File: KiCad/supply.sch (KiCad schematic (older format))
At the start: 61 parts, among them IC12 74HC00PW, IC13 SN74LVC1G126DCKR, IC4 TPS7A0518PDBVT, T3 BSS138APW, U1 LM60440AQRPKRQ1, U2 LM60440AQRPKRQ1

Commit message: Move ethernet connector closet to the edge. Loclib
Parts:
- C16, C17, C18, C19, C20, C21: footprint antmicro-footprints:0805-cap -> jetson-nano-baseboard-footprints:0805-cap; symbol antmicroCapacitorsmisc:C_47u_0805 -> jetson-nano-baseboard:C_47u_0805
- C60: footprint antmicro-footprints:0402-cap -> jetson-nano-baseboard-footprints:0402-cap; symbol antmicroCapacitors0402:C_2u2_0402 -> jetson-nano-baseboard:C_2u2_0402
- C65, C87, C88: footprint antmicro-footprints:0402-cap -> jetson-nano-baseboard-footprints:0402-cap; symbol antmicroCapacitors0402:C_1u_0402 -> jetson-nano-baseboard:C_1u_0402
- C81, C82: footprint antmicro-footprints:0603-cap -> jetson-nano-baseboard-footprints:0603-cap; symbol antmicroCapacitors0603:C_4u7_0603 -> jetson-nano-baseboard:C_4u7_0603
- C83, C84, C85, C86: footprint antmicro-footprints:0603-cap -> jetson-nano-baseboard-footprints:0603-cap; symbol antmicroCapacitors0603:C_220n_0603_25V -> jetson-nano-baseboard:C_220n_0603_25V
- C89, C90: footprint antmicro-footprints:0402-cap -> jetson-nano-baseboard-footprints:0402-cap; symbol antmicroCapacitors0402:C_100n_0402 -> jetson-nano-baseboard:C_100n_0402
- C92, C93: footprint antmicro-footprints:0402-cap -> jetson-nano-baseboard-footprints:0402-cap; symbol antmicroCapacitors0402:C_15p_0402 -> jetson-nano-baseboard:C_15p_0402
- FB3, FB4: footprint antmicro-footprints:0805-cap -> jetson-nano-baseboard-footprints:0805-cap; symbol Device:Ferrite_Bead_Small -> jetson-nano-baseboard:Ferrite_Bead_Small
- IC4: footprint antmicro-footprints:SOT-23-5 -> jetson-nano-baseboard-footprints:SOT-23-5; symbol antmicroPMICVoltageRegulatorsLinear:TPS7A0518PDBVT -> jetson-nano-baseboard:TPS7A0518PDBVT
- L11: footprint antmicro-footprints:WE_7447709150 -> jetson-nano-baseboard-footprints:WE_7447709150; symbol antmicroFixedInductors:7447709150 -> jetson-nano-baseboard:7447709150
- L12: footprint antmicro-footprints:WE_7443251000 -> jetson-nano-baseboard-footprints:WE_7443251000; symbol antmicroFixedInductors:7443251000 -> jetson-nano-baseboard:7443251000
- R117, R94: footprint antmicro-footprints:0402-res -> jetson-nano-baseboard-footprints:0402-res; symbol antmicroResistors0402:R_100k_0402 -> jetson-nano-baseboard:R_100k_0402
- R118, R120: footprint antmicro-footprints:0402 -> jetson-nano-baseboard-footprints:0402; symbol antmicroResistors0402:R_100k_1%_0402 -> jetson-nano-baseboard:R_100k_1%_0402
- R119: footprint antmicro-footprints:0402-res -> jetson-nano-baseboard-footprints:0402-res; symbol antmicroResistors0402:R_44k2_0402 -> jetson-nano-baseboard:R_44k2_0402
- R121: footprint antmicro-footprints:0402-res -> jetson-nano-baseboard-footprints:0402-res; symbol antmicroResistors0402:R_24k9_0.1%_0402 -> jetson-nano-baseboard:R_24k9_0.1%_0402
- R92: footprint antmicro-footprints:0402-res -> jetson-nano-baseboard-footprints:0402-res; symbol antmicroResistors0402:R_0R_0402 -> jetson-nano-baseboard:R_0R_0402
- U1, U2: symbol antmicroDCDCConverters:LM60440AQRPKRQ1 -> jetson-nano-baseboard:LM60440AQRPKRQ1

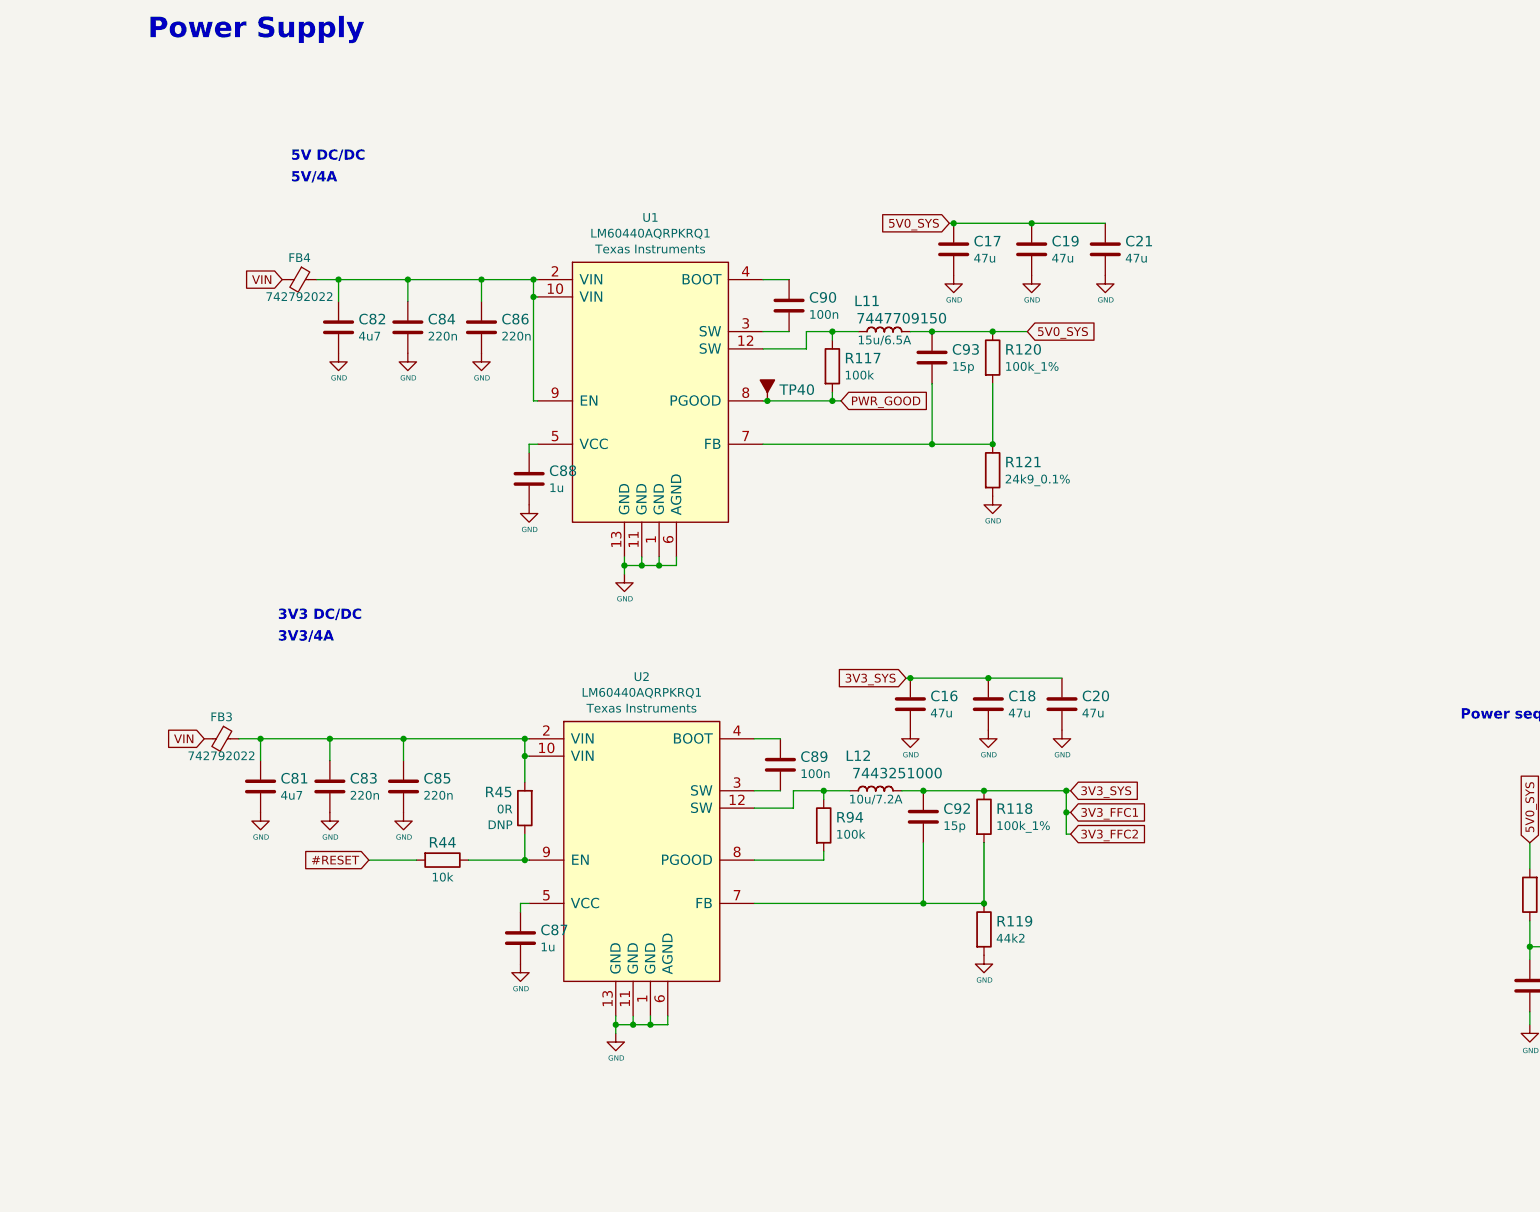
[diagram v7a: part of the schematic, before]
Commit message: Rework 3V3 and 5V DCDC on schematic, layout 3V3 DCDC
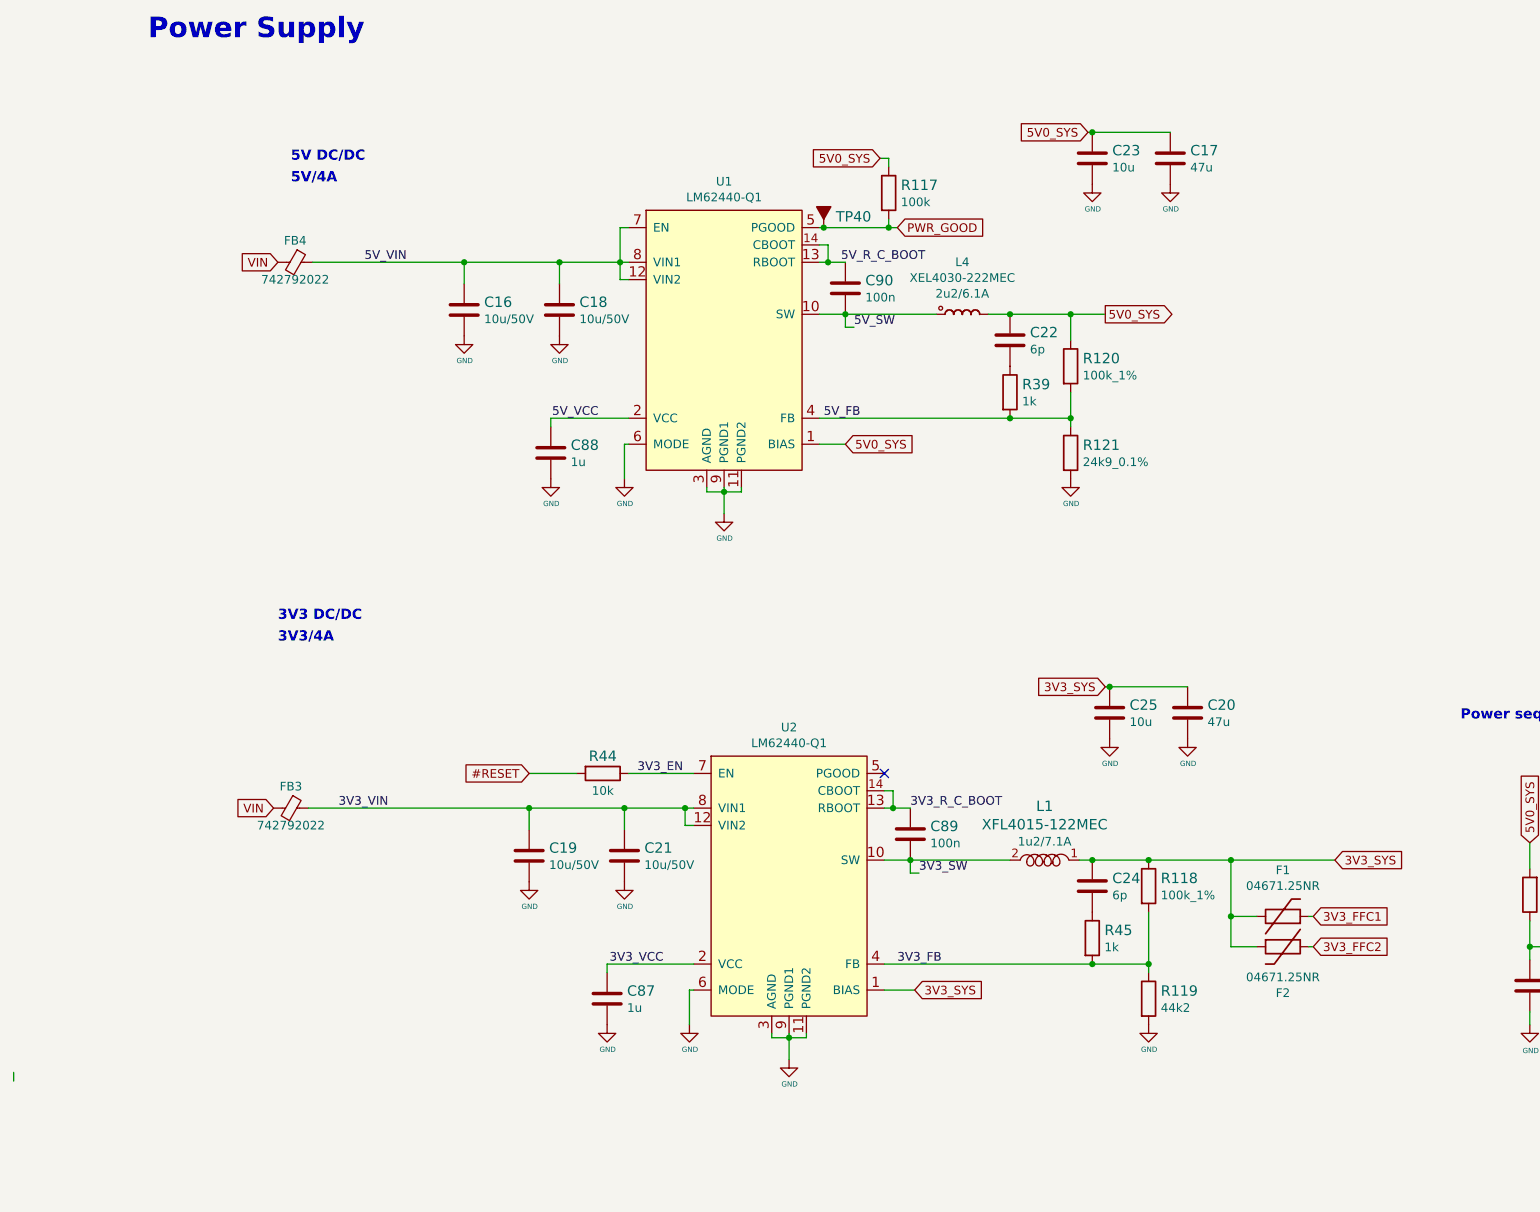
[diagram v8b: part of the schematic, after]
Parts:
- removed C16, C18, C19, C21: C_47u_0805, jetson-nano-baseboard-footprints:0805-cap, symbol jetson-nano-baseboard:C_47u_0805
- removed C81, C82: C_4u7_0603, jetson-nano-baseboard-footprints:0603-cap, symbol jetson-nano-baseboard:C_4u7_0603
- removed C83, C84, C85, C86: C_220n_0603_25V, jetson-nano-baseboard-footprints:0603-cap, symbol jetson-nano-baseboard:C_220n_0603_25V
- removed C92, C93: C_15p_0402, jetson-nano-baseboard-footprints:0402-cap, symbol jetson-nano-baseboard:C_15p_0402
- removed L11: 7447709150, jetson-nano-baseboard-footprints:WE_7447709150, symbol jetson-nano-baseboard:7447709150
- removed L12: 7443251000, jetson-nano-baseboard-footprints:WE_7443251000, symbol jetson-nano-baseboard:7443251000
- removed R45: R_0R_0402, jetson-nano-baseboard-footprints:0402-res, symbol jetson-nano-baseboard:R_0R_0402
- removed R94: R_100k_0402, jetson-nano-baseboard-footprints:0402-res, symbol jetson-nano-baseboard:R_100k_0402
- removed U1, U2: LM60440AQRPKRQ1, LM60440AQRPKRQ1, symbol jetson-nano-baseboard:LM60440AQRPKRQ1
- added C16, C18, C19, C21: C_10u_1206_50V, jetson-nano-baseboard-footprints:1206-cap, symbol jetson-nano-baseboard:C_10u_1206_50V
- added C22, C24: C_6p_0402, jetson-nano-baseboard-footprints:0402-cap, symbol jetson-nano-baseboard:C_6p_0402
- added C23, C25: C_10u_0805, jetson-nano-baseboard-footprints:0805-cap, symbol jetson-nano-baseboard:C_10u_0805
- added F1, F2: 04671.25NR, jetson-nano-baseboard-footprints:0603-Fuse-Littelfuse-0467, symbol jetson-nano-baseboard:04671.25NR
- added L1: XFL4015-122MEC, jetson-nano-baseboard-footprints:XFL4015-122MEC, symbol jetson-nano-baseboard:XFL4015-122MEC
- added L4: XEL4030-222MEC, jetson-nano-baseboard-footprints:Coilcraft-XEL4030, symbol jetson-nano-baseboard:XEL4030-222MEC
- added R39, R45: R_1k_0402, jetson-nano-baseboard-footprints:0402-res, symbol jetson-nano-baseboard:R_1k_0402
- added U1, U2: LM62440-Q1, jetson-nano-baseboard-footprints:VQFN-14-HR, symbol jetson-nano-baseboard:LM62440-Q1
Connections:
- net 3V3_FFC1: now also F1.2; no longer C20.1, R118.1
- net 5V0_SYS: now also R117.1, C22.1, C23.1, L4.2 (P), U1.1 (BIAS)
- net GND: now also C16.2, C18.2, C19.2, C21.2, C23.2, C25.2, U1.11 (PGND2), U1.3 (AGND), U1.6 (MODE), U1.9 (PGND1), U2.11 (PGND2), U2.3 (AGND), U2.6 (MODE), U2.9 (PGND1)
- net PWR_GOOD: now also U1.5 (PGOOD)
- net 5V_VIN: now reaches FB4.1
- net 5V_VIN: now also C16.1, C18.1, U1.12 (VIN2), U1.7 (EN), U1.8 (VIN1)
- net 5V_SW: now reaches C90.1
- net 5V_SW: now also L4.1 (P), U1.10 (SW)
- net 5V_R_C_BOOT: now reaches C90.2
- net 5V_R_C_BOOT: now also U1.13 (RBOOT), U1.14 (CBOOT)
- net 5V_VCC: now reaches C88.1
- net 5V_VCC: now also U1.2 (VCC)
- net 5V_FB: now reaches R120.2, R121.1
- net 5V_FB: now also R39.2, U1.4 (FB)
- net 3V3_VIN: now reaches FB3.1
- net 3V3_VIN: now also C19.1, C21.1, U2.12 (VIN2), U2.8 (VIN1)
- net 3V3_SW: now reaches C89.1
- net 3V3_SW: now also L1.2, U2.10 (SW)
- net 3V3_R_C_BOOT: now reaches C89.2
- net 3V3_R_C_BOOT: now also U2.13 (RBOOT), U2.14 (CBOOT)
- net 3V3_VCC: now reaches C87.1
- net 3V3_VCC: now also U2.2 (VCC)
- net 3V3_FB: now reaches R118.2, R119.1
- net 3V3_FB: now also R45.2, U2.4 (FB)
- net 3V3_EN: now reaches R44.1
- net 3V3_EN: now also U2.7 (EN)
- new net: C22.2, R39.1
- new net: C24.2, R45.1
- new net 3V3_FFC2: F2.1
- new net 3V3_SYS: C20.1, C24.1, C25.1, F1.1, F2.2, L1.1, R118.1, U2.1 (BIAS)
- no-connect marks 0 -> 1
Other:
- moved on the sheet: C87, C88, C89, C90, FB3, FB4, R117, R118, R119, R120, R121, R44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
